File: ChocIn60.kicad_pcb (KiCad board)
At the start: 2 copper layers, 285 x 94.6 mm, 9 parts

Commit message: シンボルとフットプリントを関連付け
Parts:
- added C1: 22pF, Capacitor_SMD:C_0603_1608Metric_Pad1.05x0.95mm_HandSolder, B.Cu at (27.0, 27.0)
- added C2: 22pF, Capacitor_SMD:C_0603_1608Metric_Pad1.05x0.95mm_HandSolder, B.Cu at (3.95, 17.8)
- added C3: 1uF, Capacitor_SMD:C_0603_1608Metric_Pad1.05x0.95mm_HandSolder, B.Cu at (8.30, 17.8)
- added C4: 0.1uF, Capacitor_SMD:C_0603_1608Metric_Pad1.05x0.95mm_HandSolder, B.Cu at (22.2, 26.2)
- added C5: 0.1uF, Capacitor_SMD:C_0603_1608Metric_Pad1.05x0.95mm_HandSolder, B.Cu at (29.6, 34.3)
- added C6: 0.1uF, Capacitor_SMD:C_0603_1608Metric_Pad1.05x0.95mm_HandSolder, B.Cu at (27.0, 29.5)
- added C7: 10uF, Capacitor_SMD:C_0603_1608Metric_Pad1.05x0.95mm_HandSolder, B.Cu at (18.2, 18.2)
- added D1: Schottky, Diode_SMD:D_SOD-123, B.Cu at (29.8, 40.2)
- added D2: PRTR5V0U2X, Package_TO_SOT_SMD:SOT-143, B.Cu at (13.9, 21.7)
- added F1: 500mA, Fuse:Fuse_1206_3216Metric_Pad1.42x1.75mm_HandSolder, B.Cu at (19.6, 32.1)
- added J1: USB_B_Micro, Connector_USB:USB_Micro-B_GCT_USB3076-30-A, B.Cu at (21.8, 38.7)
- added J2: AVR-ISP-6, Connector_PinHeader_2.54mm:PinHeader_2x03_P2.54mm_Horizontal, B.Cu at (-10.3, 39.5)
- added J3: FFC_FPC_Connectors_29POS, ChocIn60:TE_1-2013496-0, B.Cu at (7.60, 26.3)
- added J4: Conn_01x04, Connector_PinHeader_2.54mm:PinHeader_1x04_P2.54mm_Horizontal, B.Cu at (5.60, 39.5)
- added R1: 22, Resistor_SMD:R_0805_2012Metric_Pad1.15x1.40mm_HandSolder, B.Cu at (25.0, 32.2)
- added R2: 22, Resistor_SMD:R_0805_2012Metric_Pad1.15x1.40mm_HandSolder, B.Cu at (29.3, 37.0)
- added R5: 10k, Resistor_SMD:R_0805_2012Metric_Pad1.15x1.40mm_HandSolder, B.Cu at (22.4, 28.9)
- added R6: 4.7k, Resistor_SMD:R_0805_2012Metric_Pad1.15x1.40mm_HandSolder, B.Cu at (13.7, 17.9)
- added R7: 4.7k, Resistor_SMD:R_0805_2012Metric_Pad1.15x1.40mm_HandSolder, B.Cu at (18.9, 22.5)
- added SW1: SW_Push, Orbit_locallib:SKQGADE010, B.Cu at (6.55, 22.3)
- added U1: ATmega32U4-AU, Package_QFP:TQFP-44_10x10mm_P0.8mm, B.Cu at (-5.45, 24.9)
- added Y1: 16MHz, Crystal:Crystal_SMD_3225-4Pin_3.2x2.5mm_HandSoldering, B.Cu at (16.8, 26.8)

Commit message: 差動ペアを引いてみた
が、これでよいのかわからん。
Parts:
- D2: footprint Package_TO_SOT_SMD:SOT-143 -> Orbit_locallib:SOT143B
- moved U1 113.6 mm to (95.2, 77.5)
- moved SW1 98.4 mm to (69.1, 98.2), turned to 180 degrees
- moved D2 57.3 mm to (57.9, 58.5), turned to 270 degrees
- moved R1 47.4 mm to (59.5, 64.8), turned to 90 degrees
- moved J1 39.0 mm to (58.2, 52.7)
- moved R2 38.7 mm to (56.3, 64.8), turned to 90 degrees
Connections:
- net Net-(D2-Pad2) renamed /DP
- net Net-(D2-Pad3) renamed /DN
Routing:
- net D+: track 0.00 -> 40.4 mm
- net D-: track 0.00 -> 40.4 mm
- net /DP: track 0.00 -> 10.9 mm
- net /DN: track 0.00 -> 10.9 mm

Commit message: [WIP] 電源周り配線
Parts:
- moved D1 47.3 mm to (49.5, 83.2), turned to 90 degrees
- moved F1 40.4 mm to (51.0, 57.7)
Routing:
- net VBUS: track 0.00 -> 78.0 mm, vias 0 -> 2
- net VCC: track 0.00 -> 7.98 mm
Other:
- net class V added: clearance 0.2, trace_width 0.5, via_dia 0.8, via_drill 0.4
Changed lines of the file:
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@@
     (thickness 1.6)
     (drawings 246)
-    (tracks 68)
+    (tracks 84)
     (zones 0)
     (modules 31)
@@
     (47 F.CrtYd user)
     (48 B.Fab user)
-    (49 F.Fab user hide)
+    (49 F.Fab user)
   )
   (setup
@@
     (solder_mask_min_width 0.25)
     (aux_axis_origin 0 0)
-    (visible_elements 7FFFF7FF)
+    (visible_elements 7FFFFFFF)
     (pcbplotparams
       (layerselection 0x010fc_ffffffff)
@@
     (uvia_dia 0.3)
     (uvia_drill 0.1)
-    (add_net +5V)
     (add_net /DN)
     (add_net /DP)
@@
     (add_net PF6)
     (add_net PF7)
+    (add_net ~RESET)
+  )
+  (net_class V ""
+    (clearance 0.2)
+    (trace_width 0.5)
+    (via_dia 0.8)
+    (via_drill 0.4)
+    (uvia_dia 0.3)
+    (uvia_drill 0.1)
+    (add_net +5V)
     (add_net VBUS)
     (add_net VCC)
-    (add_net ~RESET)
   )
   (module Orbit_locallib:SOT143B (layer B.Cu)
@@
   )
   (module Fuse:Fuse_1206_3216Metric_Pad1.42x1.75mm_HandSolder (layer B.Cu)
-    (at 19.65 32.07)
+    (at 50.9635 57.658)
     (descr "Fuse SMD 1206 (3216 Metric), square (rectangular) end terminal, IPC_7351 nominal with elongated pad for handsoldering. (Body size source: http://www.tortai-tech.com/upload/download/2011102023233369053.pdf), generated with kicad-footprint-generator")
     (tags "resistor handsolder")
@@
   )
   (module Diode_SMD:D_SOD-123 (layer B.Cu)
-    (at 29.8 40.19)
+    (at 49.53 83.185 90)
     (descr SOD-123)
     (tags SOD-123)
     (attr smd)
-    (fp_text reference D1 (at 0 2) (layer B.SilkS)
-      (effects (font (size 1 1) (thickness 0.15)) (justify mirror))
-    )
-    (fp_text value Schottky (at 0 -2.1) (layer B.Fab)
+    (fp_text reference D1 (at 0 2 90) (layer B.SilkS)
+      (effects (font (size 1 1) (thickness 0.15)) (justify mirror))
+    )
+    (fp_text value Schottky (at 0 -2.1 90) (layer B.Fab)
       (effects (font (size 1 1) (thickness 0.15)) (justify mirror))
     )
@@
     (fp_line (start 0.25 0) (end 0.75 0) (layer B.Fab) (width 0.1))
     (fp_line (start -2.25 1) (end -2.25 -1) (layer B.SilkS) (width 0.12))
-    (fp_text user %R (at 0 2) (layer B.Fab)
-      (effects (font (size 1 1) (thickness 0.15)) (justify mirror))
-    )
-    (pad 2 smd rect (at 1.65 0) (size 0.9 1.2) (layers B.Cu B.Paste B.Mask)
+    (fp_text user %R (at 0 2 90) (layer B.Fab)
+      (effects (font (size 1 1) (thickness 0.15)) (justify mirror))
+    )
+    (pad 2 smd rect (at 1.65 0 90) (size 0.9 1.2) (layers B.Cu B.Paste B.Mask)
       (net 6 VBUS))
-    (pad 1 smd rect (at -1.65 0) (size 0.9 1.2) (layers B.Cu B.Paste B.Mask)
+    (pad 1 smd rect (at -1.65 0 90) (size 0.9 1.2) (layers B.Cu B.Paste B.Mask)
       (net 5 +5V))
     (model ${KISYS3DMOD}/Diode_SMD.3dshapes/D_SOD-123.wrl
@@
   (gr_line (start 30 86.2) (end 334 86.2) (angle 90) (layer Eco1.User) (width 0.381))
   (gr_line (start 334 107.5) (end 30 107.5) (angle 90) (layer Eco1.User) (width 0.381))
+  (segment (start 49.476 57.658) (end 49.476 81.481) (width 0.5) (layer B.Cu) (net 6))
+  (segment (start 49.53 81.535) (end 59.945 81.535) (width 0.5) (layer B.Cu) (net 6))
+  (segment (start 62.23 83.82) (end 66.675 83.82) (width 0.5) (layer B.Cu) (net 6))
+  (segment (start 66.675 83.82) (end 68.58 81.915) (width 0.5) (layer B.Cu) (net 6))
+  (segment (start 68.58 81.915) (end 78.105 81.915) (width 0.5) (layer B.Cu) (net 6))
+  (segment (start 59.945 81.535) (end 62.23 83.82) (width 0.5) (layer B.Cu) (net 6))
+  (segment (start 78.105 81.915) (end 79.35 80.67) (width 0.5) (layer B.Cu) (net 6))
+  (segment (start 89.55 76.67) (end 83.35 76.67) (width 0.5) (layer B.Cu) (net 6))
+  (via (at 83.35 76.67) (size 0.8) (drill 0.4) (layers F.Cu B.Cu) (net 6))
+  (segment (start 79.35 80.67) (end 89.55 80.67) (width 0.5) (layer B.Cu) (net 6))
+  (via (at 79.35 80.67) (size 0.8) (drill 0.4) (layers F.Cu B.Cu) (net 6))
+  (segment (start 79.35 80.67) (end 83.35 76.67) (width 0.5) (layer F.Cu) (net 6))
+  (segment (start 56.9 57.5005) (end 56.8739 57.5266) (width 0.4) (layer B.Cu) (net 7))
+  (segment (start 56.9 54.15) (end 56.9 57.5005) (width 0.4) (layer B.Cu) (net 7))
+  (segment (start 52.2919 57.5266) (end 52.2875 57.531) (width 0.5) (layer B.Cu) (net 7))
+  (segment (start 56.8739 57.5266) (end 52.2919 57.5266) (width 0.5) (layer B.Cu) (net 7))
   (segment (start 88.424999 79.07) (end 89.55 79.07) (width 0.2) (layer B.Cu) (net 36))
   (segment (start 88.249999 79.245) (end 88.424999 79.07) (width 0.2) (layer B.Cu) (net 36))

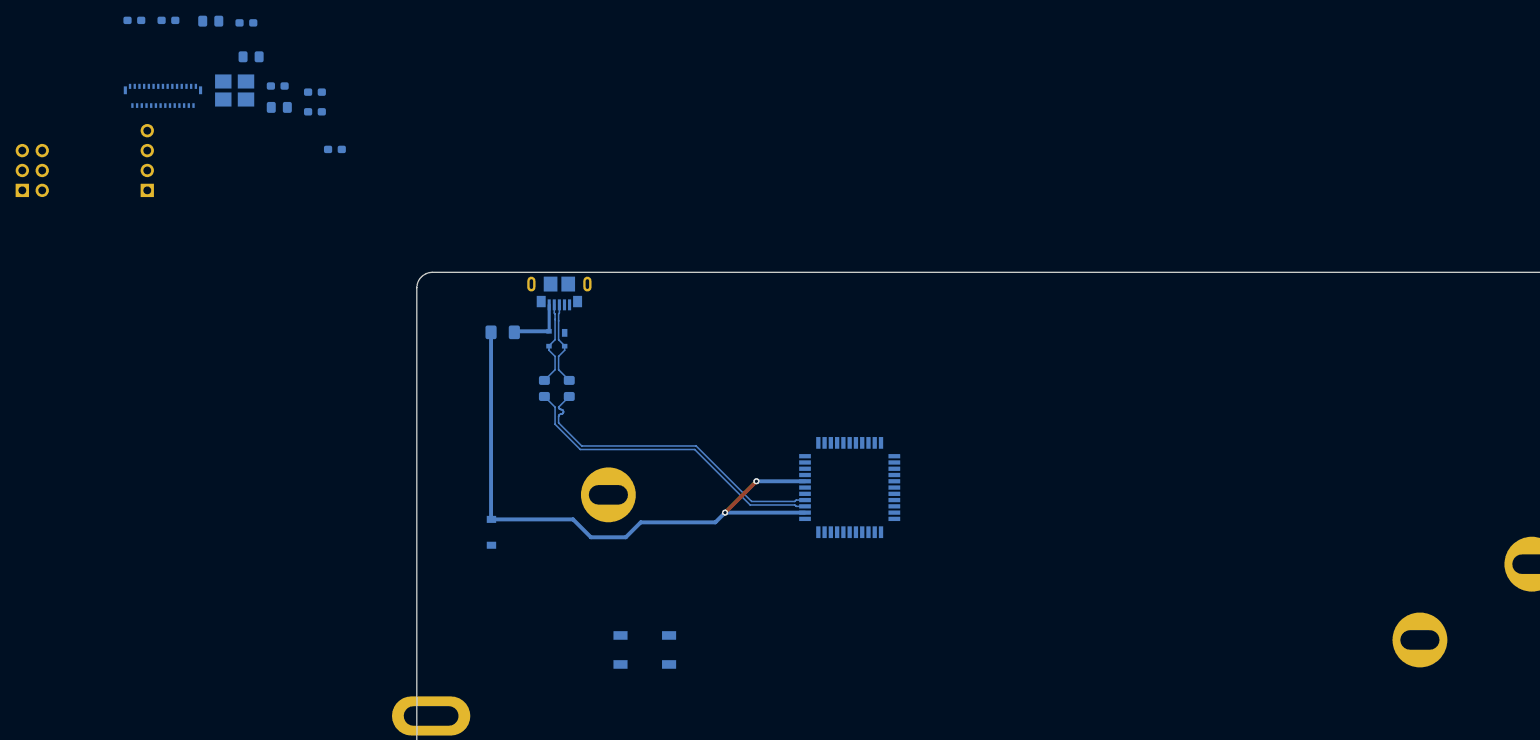
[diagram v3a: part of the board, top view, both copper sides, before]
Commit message: [WIP] 配線とGNDベタ
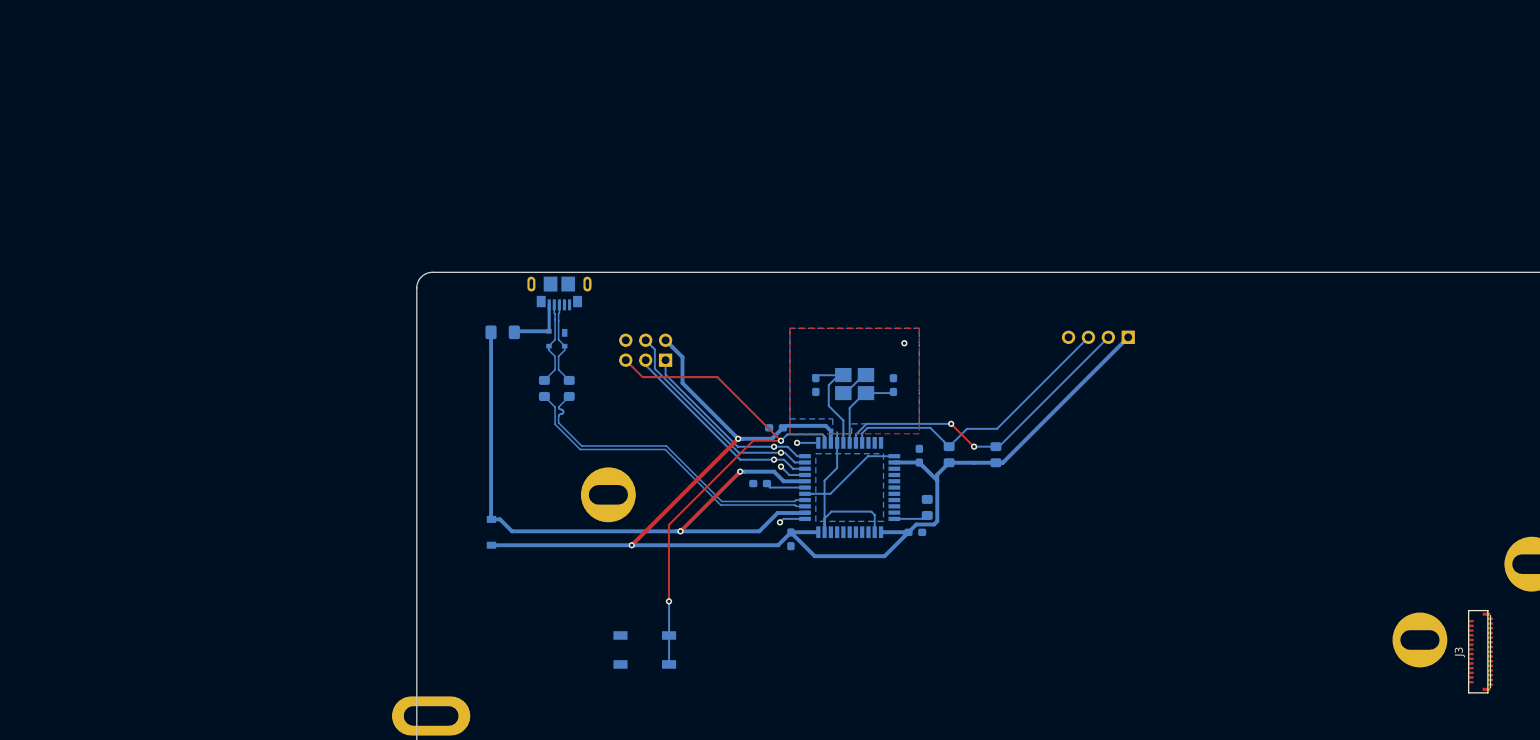
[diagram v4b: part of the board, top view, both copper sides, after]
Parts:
- J3: moved to F.Cu
- moved J3 184.2 mm to (177.0, 98.4), turned to 90 degrees
- moved J4 126.6 mm to (130.8, 58.3), turned to 90 degrees
- moved R6 114.5 mm to (113.9, 73.3), turned to 90 degrees
- moved R7 102.6 mm to (108.0, 73.3), turned to 90 degrees
- moved C2 98.7 mm to (90.9, 64.4), turned to 270 degrees
- moved R5 97.2 mm to (105.2, 80.0), turned to 270 degrees
- moved C3 95.9 mm to (83.8, 77.0), turned to 180 degrees
- moved C7 95.8 mm to (87.8, 84.1), turned to 270 degrees
- moved C6 88.8 mm to (104.1, 73.4), turned to 270 degrees
- moved C5 88.8 mm to (103.6, 83.2)
- moved Y1 87.6 mm to (95.9, 64.3), turned to 180 degrees
- moved J2 84.9 mm to (71.8, 61.2), turned to 90 degrees
- moved C1 82.8 mm to (100.8, 64.4), turned to 90 degrees
- moved C4 77.1 mm to (85.9, 69.8)
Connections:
- U1 pad 14: GND -> +5V
- U1 pad 24: GND -> +5V
- U1 pad 34: GND -> +5V
- U1 pad 44: GND -> +5V
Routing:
- net +5V: track 0.00 -> 161.1 mm, vias 0 -> 2
- net ~RESET: track 0.00 -> 67.5 mm, vias 0 -> 2
- net GND: track 0.00 -> 41.5 mm, vias 0 -> 1
- net PD0_SCL: track 0.00 -> 40.8 mm, vias 0 -> 2
- net PD1_SDA: track 0.00 -> 37.2 mm
- net PB2_MOSI: track 0.00 -> 28.2 mm, vias 0 -> 1
- net PB1_SCK: track 0.00 -> 26.4 mm, vias 0 -> 1
- net PB3_MISO: track 0.00 -> 23.9 mm, vias 0 -> 1
- net Net-(C2-Pad1): track 0.00 -> 14.4 mm
- net Net-(C1-Pad1): track 0.00 -> 11.1 mm
- net VBUS: track 78.0 -> 86.0 mm
- net Net-(C3-Pad1): track 0.00 -> 5.18 mm
- net Net-(R5-Pad2): track 0.00 -> 4.46 mm
- net PB0: track 0.00 -> 3.50 mm, vias 0 -> 1
- net PE6: track 0.00 -> 3.37 mm, vias 0 -> 1
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- added copper zone on B.Cu, net GND
- added copper zone on F.Cu, net GND
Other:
- board text removed: "W"

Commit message: とりあえず、	USBとATmega32U4の周りだけ切り出してみる
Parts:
- J3: value FFC_FPC_Connectors_29POS -> Conn_01x30; footprint ChocIn60:TE_1-2013496-0 -> Connector_PinSocket_2.54mm:PinSocket_2x15_P2.54mm_Vertical; moved to B.Cu
- moved J3 94.5 mm to (82.5, 101.6), turned to 270 degrees
- moved R5 0.51 mm to (105.7, 80.0)
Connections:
- J3 pad 10: PB6 -> PF0
- J3 pad 11: PB7 -> PF1
- J3 pad 12: PC6 -> PF4
- J3 pad 13: PC7 -> PF5
- J3 pad 14: PD0_SCL -> PF6
- J3 pad 15: PD1_SDA -> PF7
- J3 pad 16: PD2 -> PB5
- J3 pad 17: PD3 -> PB6
- J3 pad 18: PD4 -> PC7
- J3 pad 19: PD5 -> PC6
- J3 pad 20: PD6 -> PB4
- J3 pad 22: PE6 -> PD6
- J3 pad 23: PF0 -> PD4
- J3 pad 24: PF1 -> PD5
- J3 pad 25: PF4 -> PD3
- J3 pad 26: PF5 -> PD2
- J3 pad 27: PF6 -> PD0_SCL
- J3 pad 28: PF7 -> PD1_SDA
- J3 pad 6: PB2_MOSI -> PE6
- J3 pad 8: PB4 -> PB2_MOSI
- J3 pad 9: PB5 -> PB7
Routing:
- net GND: track 41.5 -> 98.9 mm, vias 1 -> 31
- net PD0_SCL: track 40.8 -> 89.7 mm
- net PD1_SDA: track 37.2 -> 83.3 mm
- net PB3_MISO: track 23.9 -> 70.0 mm
- net PD3: track 0.00 -> 41.3 mm, vias 0 -> 1
- net PD2: track 0.00 -> 40.7 mm, vias 0 -> 1
- net PB1_SCK: track 26.4 -> 65.1 mm
- net PD5: track 0.00 -> 34.8 mm, vias 0 -> 1
- net PD4: track 0.00 -> 33.7 mm, vias 0 -> 1
- net +5V: track 161.1 -> 194.5 mm
- net PB7: track 2.72 -> 34.6 mm
- net PD7: track 0.00 -> 30.7 mm, vias 0 -> 1
- net PD6: track 0.00 -> 29.3 mm, vias 0 -> 1
- net PB6: track 0.00 -> 27.7 mm, vias 0 -> 1
- net PB2_MOSI: track 28.2 -> 55.8 mm
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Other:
- board size 285 x 94.6 mm -> 100 x 70 mm
- rule trace_min: 0.2 -> 0
- board text removed: "CAPS"
- board text removed: "D"
- board text removed: "ESC"
- board text removed: "S"

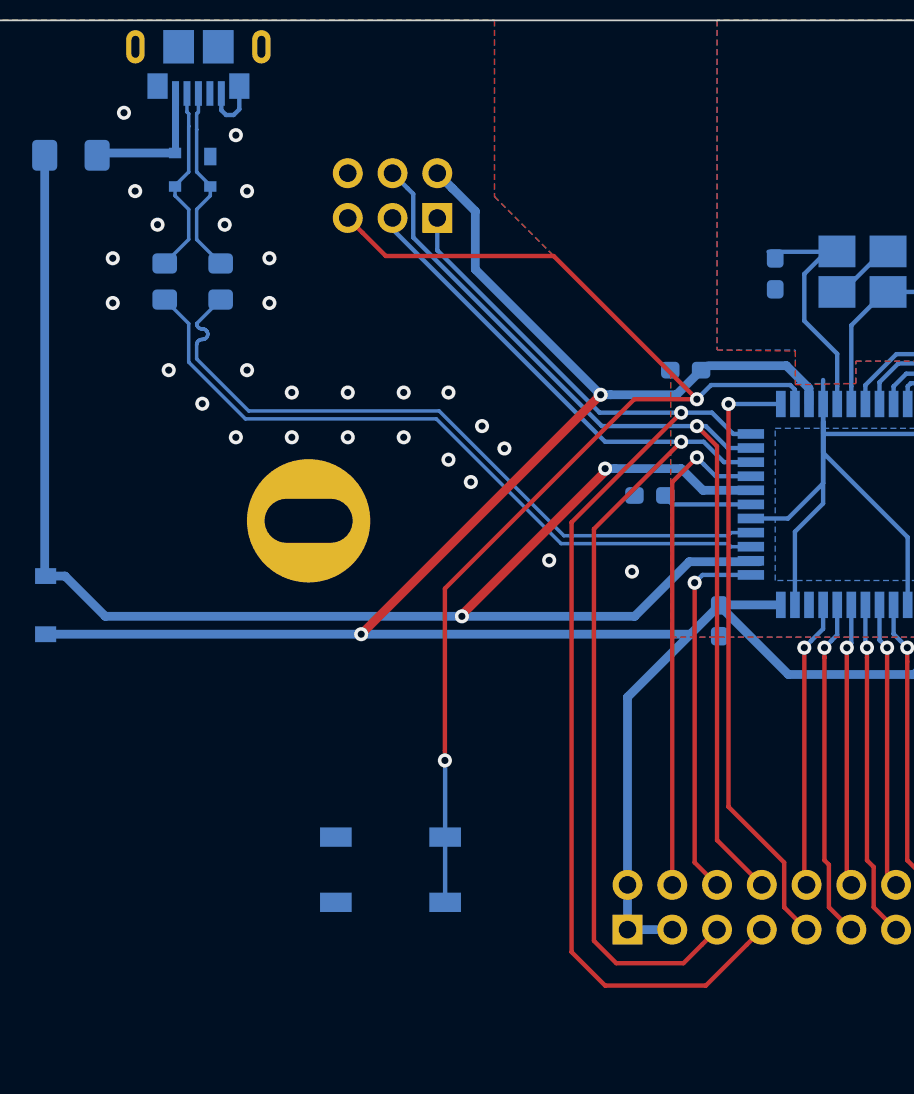
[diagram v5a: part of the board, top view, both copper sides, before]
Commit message: USBの信号線の下にほかの配線はNG
https://discordapp.com/channels/376937950409392130/380697359316942848/602687426242019328
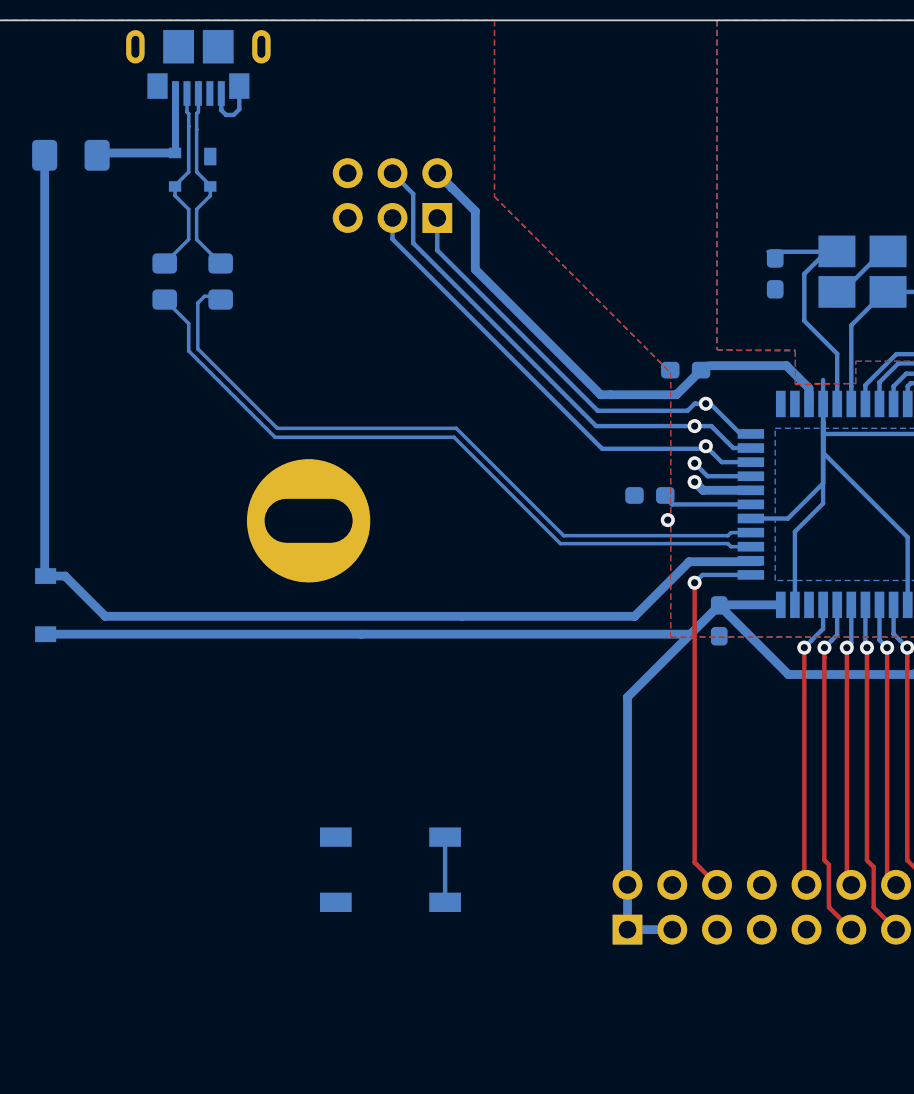
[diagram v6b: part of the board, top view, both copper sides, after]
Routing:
- net ~RESET: track 67.5 -> 3.70 mm, vias 2 -> 0
- net PB3_MISO: track 70.0 -> 24.3 mm
- net PB1_SCK: track 65.1 -> 26.9 mm
- net PB7: track 34.6 -> 0.00 mm, vias 1 -> 0
- net PB2_MOSI: track 55.8 -> 28.4 mm
- net PB0: track 28.3 -> 3.49 mm
- net +5V: track 194.5 -> 175.3 mm, vias 2 -> 0
- net VBUS: track 87.6 -> 70.4 mm, vias 2 -> 1
- net GND: vias 31 -> 5
